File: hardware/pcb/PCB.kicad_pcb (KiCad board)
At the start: 2 copper layers, 55 x 95 mm, 47 parts, among them J1 USB_A, J2 AudioJack3, J3 USB_B_Micro, Q1 BSS138, Q2 MMBT3904, Q3 MMBT3904, SW1 RESET, SW2 S4, SW3 BOOT, SW4 RESET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

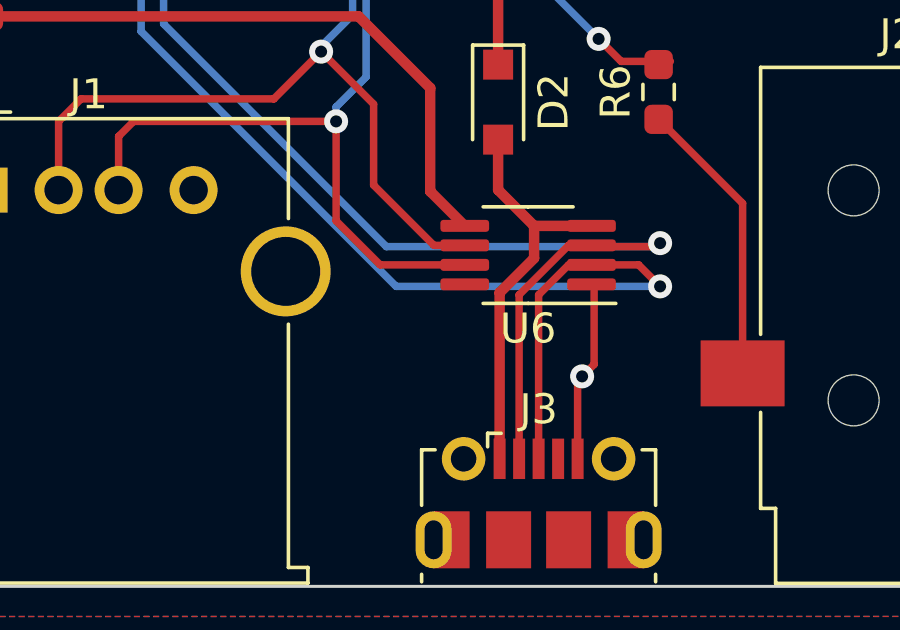
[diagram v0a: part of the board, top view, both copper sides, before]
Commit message: add GND via
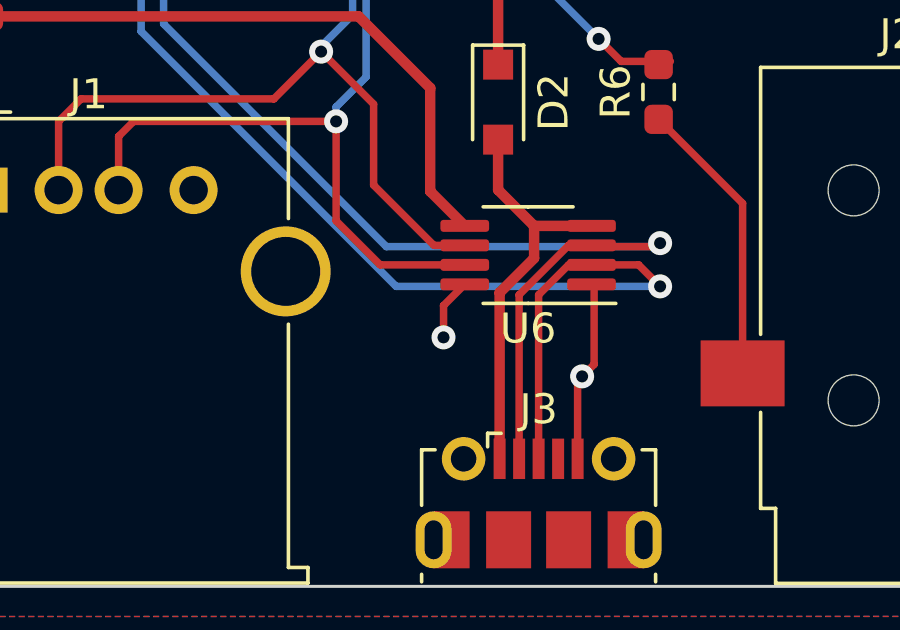
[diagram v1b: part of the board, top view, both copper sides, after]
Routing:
- net GND: track 154.1 -> 156.2 mm, vias 21 -> 22
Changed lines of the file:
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@@
     (fp_line (start 15.773 -4.623) (end 16.789 -4.623) (layer "F.Fab") (width 0.1))
     (fp_arc (start 15.4683 -1.77807) (mid 15.337791 -1.66395) (end 15.189 -1.57497) (layer "F.Fab") (width 0.1))
-    (fp_arc (start 15.7741 -2.43797) (mid 15.681428 -2.080032) (end 15.4692 -1.77727) (layer "F.Fab") (width 0.1))
-    (fp_arc (start 16.7899 -2.43818) (mid 16.198173 -1.073815) (end 14.8338 -0.482103) (layer "F.Fab") (width 0.1))
+    (fp_arc (start 15.7741 -2.43797) (mid 15.681421 -2.080038) (end 15.4692 -1.77727) (layer "F.Fab") (width 0.1))
+    (fp_arc (start 16.7899 -2.43818) (mid 16.198174 -1.073812) (end 14.8338 -0.482103) (layer "F.Fab") (width 0.1))
     (fp_arc (start 14.8587 -1.49811) (mid 14.846 -1.497996) (end 14.8333 -1.49811) (layer "F.Fab") (width 0.1))
-    (fp_arc (start 15.1891 -1.57484) (mid 15.101269 -1.545512) (end 15.0112 -1.52402) (layer "F.Fab") (width 0.1))
+    (fp_arc (start 15.1891 -1.57484) (mid 15.101269 -1.545515) (end 15.0112 -1.52402) (layer "F.Fab") (width 0.1))
     (fp_arc (start 14.9094 -1.49828) (mid 14.884 -1.498001) (end 14.8586 -1.49828) (layer "F.Fab") (width 0.1))
     (fp_arc (start 1.01654 -0.48323) (mid 0.720001 -0.991) (end 1.01654 -1.49877) (layer "F.Fab") (width 0.1))
-    (fp_arc (start 15.0114 -1.52338) (mid 14.960879 -1.509562) (end 14.9098 -1.49798) (layer "F.Fab") (width 0.1))
+    (fp_arc (start 15.0114 -1.52338) (mid 14.960879 -1.509563) (end 14.9098 -1.49798) (layer "F.Fab") (width 0.1))
     (pad "H201" smd rect (at 12 -19.175 180) (size 1.27 0.889) (layers "F.Cu" "F.Paste" "F.Mask")
       (net 59 "unconnected-(U3-PadH201)") (pinfunction "SWDIO") (pintype "passive+no_connect"))
@@
   (segment (start 131.6 172.6) (end 131.6 170.0205) (width 0.25) (layer "F.Cu") (net 6))
   (segment (start 107.1 122.3) (end 107.1 123.9375) (width 0.25) (layer "F.Cu") (net 6))
+  (segment (start 126.58 171.7) (end 126.58 170.6405) (width 0.25) (layer "F.Cu") (net 6))
   (segment (start 107.14 118.11) (end 107.14 118.89) (width 0.25) (layer "F.Cu") (net 6))
   (segment (start 111.4375 123.9375) (end 110.4 123.9375) (width 0.25) (layer "F.Cu") (net 6))
@@
   (segment (start 113.96 111.1) (end 110.65 111.1) (width 0.25) (layer "F.Cu") (net 6))
   (segment (start 150.75 170.6125) (end 148.8875 170.6125) (width 0.25) (layer "F.Cu") (net 6))
+  (segment (start 126.58 170.6405) (end 127.2875 169.933) (width 0.25) (layer "F.Cu") (net 6))
   (segment (start 125 145.8) (end 124.4 145.2) (width 0.25) (layer "F.Cu") (net 6))
   (segment (start 112.2 131.1) (end 112.2 132.7375) (width 0.25) (layer "F.Cu") (net 6))
@@
   (via (at 142.5 136.5) (size 0.8) (drill 0.4) (layers "F.Cu" "B.Cu") (free) (net 6))
   (via (at 129.5 154.5) (size 0.8) (drill 0.4) (layers "F.Cu" "B.Cu") (free) (net 6))
+  (via (at 126.58 171.7) (size 0.8) (drill 0.4) (layers "F.Cu" "B.Cu") (free) (net 6))
   (via (at 112.2 131.1) (size 0.8) (drill 0.4) (layers "F.Cu" "B.Cu") (free) (net 6))
   (via (at 107.1 122.3) (size 0.8) (drill 0.4) (layers "F.Cu" "B.Cu") (free) (net 6))
